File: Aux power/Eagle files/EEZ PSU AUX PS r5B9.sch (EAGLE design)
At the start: 78 parts, among them IC16 LM25575, IC17 MC7812, IC18 TPD4E002DRLR, IC19 TPD2E001DZDR, IC20 ADUM3160BRWZ, Q20 BTA26-600, Q21 BTA26-600, Q22 IRLL014N, X10 826629-5, X11 2411-01, X4 282836-5, X5 09185067324, X6 22-23-2031, X7 LMJ2138812S0LOT6C, X8 826629-8, X9 826629-5

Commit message: AUX PS r5B9
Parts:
- removed B1: DF01S, rectifier:DF01S
- removed C104: 100n, rcl:C-EUC0603
- removed C84: 6n8 (X1), rcl:C-EU102-064X133
- removed FB7: 60R@100MHz, MyLib6:FERRITE_BEAD0603
- removed IC20: ADUM3160BRWZ, MyLib6:ADUM3160BRWZWIDE
- removed R102: 15R/7W, EEZ_Lib1:R_EU7W
- removed R103, R106: 330R/2W, rcl:R-EU_R2512
- removed R104: 270R, rcl:R-EU_R0805
- removed R105: 150R/2W, rcl:R-EU_R2512
- added FB4: 60R@100MHz, MyLib6:FERRITE_BEAD0603
- added R122: 2K2, rcl:R-EU_R0805
- added R123: 16K, rcl:R-EU_R0805
- added R124, R125, R131: 10K, rcl:R-EU_R0805
- added R126: 1K8, rcl:R-EU_R0805
- added R127: 100R, rcl:R-EU_R0805
- added R128: 47K, rcl:R-EU_R0805
- added R129: 1K, rcl:R-EU_R0805
- added R130: 5K6, rcl:R-EU_R0805
- added R132, R133: 22R, rcl:R-EU_R0805
- C85: value 47n/400V -> 6n8 (X1); device rcl:C-EU075-052X106 -> rcl:C-EU102-064X133
- C86: value 22n -> 47n/400V; device rcl:C-EUC0805 -> rcl:C-EU075-052X106
- C87: value 4u7 -> 22n; device rcl:C-EUC1210 -> rcl:C-EUC0805
- C88: value 1mF/25V -> 4u7; device EEZ_Lib1:ECAP5G_10.5MM -> rcl:C-EUC1210
- C91: device rcl:C-EUC0805 -> rcl:C-EUC0603
- C97: value 10u -> 100u; device MyLib6:ECAPPANASONIC_C -> EEZ_Lib1:ECAPPANASONIC_H
- C98: value 100u -> 47n; device EEZ_Lib1:ECAPPANASONIC_H -> rcl:C-EUC0805
- C99: value 47n -> 100n; device rcl:C-EUC0805 -> rcl:C-EUC0603
- IC16: value LM25575 -> LM25575MH/NOPB
- IC17: value MC7812 -> TPD4E002DRLR; device EEZ_Lib1:MC78XX -> EEZ_Lib1:TPD4E002DRLR
- IC18: value TPD4E002DRLR -> TPD2E001DZDR; device EEZ_Lib1:TPD4E002DRLR -> EEZ_Lib1:TPD2E001DZDR
- IC19: value TPD2E001DZDR -> ADUM3160BRWZ; device EEZ_Lib1:TPD2E001DZDR -> MyLib6:ADUM3160BRWZWIDE
- L9: value 100uH (MSS1260-104K) -> 100uH
- R107: value 270R -> 15R/7W; device rcl:R-EU_R0805 -> EEZ_Lib1:R_EU7W
- R108: value 15K -> 330R/2W; device rcl:R-EU_R0805 -> rcl:R-EU_R2512
- R109: value 2K2 -> 330R/2W; device rcl:R-EU_R0805 -> rcl:R-EU_R2512
- R110: value 10R -> 2K2; device rcl:R-EU_R1206 -> rcl:R-EU_R0805
- R111: value 5K6 1% -> 2K2
- R112: value 18K -> 330R/2W; device rcl:R-EU_R0805 -> rcl:R-EU_R2512
- R113: value 20K -> 49R9
- R114: value 1K8 1% -> 220R
- R115: value 100R -> 330R/2W; device rcl:R-EU_R0805 -> rcl:R-EU_R2512
- R116: value 47K -> 49R9
- R117: value 1K -> 220R
- R118: value 5K6 -> 16K
- R119: value 10K -> 2K2
- R120: value 22R -> 10R; device rcl:R-EU_R0805 -> rcl:R-EU_R1206
- R121: value 22R -> 5K6
- TR2: value TEZ6/D230/15V -> VTX-214-005-112 (or MYRRA 47154); device EEZ_Lib1:PCB_TRAFO6VA_TEZ+VPP+MYRRA -> EEZ_Lib1:AC_DC_ADAPTER_5W
- X4: value 282836-5 -> 39303055; device EEZ_Lib1:TBLOCK5.0_5A -> EEZ_Lib1:MINIFIT_6659-5
- X7: value LMJ2138812S0LOT6C -> LMJ2138814S0L1T1C; device EEZ_Lib1:RJ45-VERT -> EEZ_Lib1:RJ45-VERTLMJ2138814S0L1T1C
- renumbered U$13 to FM3, U$14 to FM4
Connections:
- removed net 12VDC: C97.+, C98.+, D20.C, IC17.VO, X6-1.S
- removed net N$78: B1.AC1, TR2.S1
- removed net N$80: B1.AC2, TR2.S2
- removed net N$82: Q21.A2, R102.2, R103.2, R105.1, X4-3.1
- new net N$152: Q20.A1, R107.2, R110.1
- new net N$169: R122.1, R123.2
- new net N$171: R124.2, R125.1
- new net N$174: OK2.C, R116.1
- new net N$175: OK1.C, R113.1
- net +5V: now also C99.1, IC19.VBUS2, R121.1, R130.1; no longer C100.1, IC20.VBUS2, R111.1, R118.1
- net AC_EARTH: now also FB6.1; no longer FB7.1
- net AC_IN1_MAIN: now also C85.1, R107.1, R111.2, TR2.IN2; no longer C84.1, Q20.A1, TR2.P2
- net AC_IN2_MAIN: now also C85.2, C86.1, TR2.IN1; no longer C84.2, C85.1, TR2.P1
- net AUX_+3V3: now also FB4.2; no longer FB5.2
- net AUX_ETH_IN+: now also IC17.IO3; no longer IC18.IO4
- net AUX_ETH_IN-: now also IC17.IO4; no longer IC18.IO3
- net AUX_ETH_OUT+: now also IC17.IO1; no longer IC18.IO2
- net AUX_ETH_OUT-: now also IC17.IO2; no longer IC18.IO1
- net AUX_FAN_CTRL: now also R127.2; no longer R115.2
- net AUX_FAN_SENSE: now also R130.2, R131.1; no longer R118.2, R119.1
- net AUX_PWR_DIRECT: now also R114.2; no longer R104.2
- net AUX_PWR_SSTART: now also R117.2; no longer R107.2
- net D+: now also IC18.IO1, R133.1; no longer IC19.IO1, R121.1
- net D-: now also IC18.IO2, R132.1; no longer IC19.IO2, R120.1
- net DC_PREG2: now also C88.1, R118.2; no longer C87.1, R108.2
- net FAN_OUT: now also C98.2; no longer C99.2
- net GND: now also C102.2, C88.2, C99.2, IC19.GND2, IC19.GND2_2, R119.1, R122.2, R126.2, R128.1, R129.1, R131.2, TR2.-; no longer B1.-, C100.2, C103.2, C87.2, C88.-, C97.-, IC18.GND, IC20.GND2, IC20.GND2_2, R109.1, R112.2, R114.2, R116.1, R117.1, R119.2
- net IS1: now also R120.1; no longer R110.1
- net MCU_D+: now also IC19.DD+; no longer IC20.DD+
- net MCU_D-: now also IC19.DD-; no longer IC20.DD-
- net N$125: now also FB4.1; no longer FB5.1
- net N$52: now also R125.2; no longer R113.2
- net N$57: now also R121.2, R126.1; no longer R111.2, R114.1
- net N$58: now also C87.2; no longer C86.2
- net N$59: now also R124.1; no longer R113.1
- net N$60: now also R123.1; no longer R112.1
- net N$69: now also R118.1, R119.2; no longer R108.1, R109.2
- net N$70: now also R120.2; no longer R110.2
- net N$71: now also R111.1
- net N$72: now also R110.2
- net N$73: now also R115.1; no longer R106.1
- net N$74: now also R113.2, R114.1; no longer OK1.C, R104.1
- net N$75: now also R116.2, R117.1; no longer OK2.C, R107.1
- net N$76: now also R112.1; no longer R103.1
- net N$81: now also Q21.A2, R108.1, R109.1, R112.2, R115.2, X4-3.1; no longer R102.1, R106.2
- net N$83: now also C86.2, R108.2, R109.2; no longer C85.2, R105.2
- net N$84: now also C98.1, R129.2; no longer C99.1, R117.2
- net N$85: now also R127.1, R128.2; no longer R115.1, R116.2
- net N$86: now also C97.-; no longer C98.-
- net N$87: now also C103.1, IC19.PDEN, IC19.SPU, IC19.VDD1; no longer C104.1, IC20.PDEN, IC20.SPU, IC20.VDD1
- net N$88: now also IC19.UD-, R132.2; no longer IC20.UD-, R120.2
- net N$89: now also IC19.UD+, R133.2; no longer IC20.UD+, R121.2
- net N$90: now also C100.1, FB5.2, IC19.VBUS1; no longer C101.1, FB6.2, IC20.VBUS1
- net N$91: now also C102.1, IC19.PIN, IC19.SPD, IC19.VDD2; no longer C103.1, IC20.PIN, IC20.SPD, IC20.VDD2
- net SW2: now also C87.1; no longer C86.1
- net VIN: now also C97.+, D20.C, TR2.+, X6-1.S; no longer B1.+, C88.+, IC17.VI
- net XUSB_GND: now also C100.2, C101.1, C103.2, FB6.2, IC18.GND, IC19.GND1, IC19.GND1_2; no longer C101.2, C102.1, C104.2, FB7.2, IC19.GND, IC20.GND1, IC20.GND1_2
- net XUSB_VBUS: now also C101.2, FB5.1, IC18.VCC; no longer C102.2, FB6.1, IC19.VCC
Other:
- note added: "SRU1038-101Y or DE1207-100"
- note removed: "or DE1207-100"
- moved on the sheet: C100, C101, C102, C103, C85, C86, C87, C90, C91, C92, C93, C94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

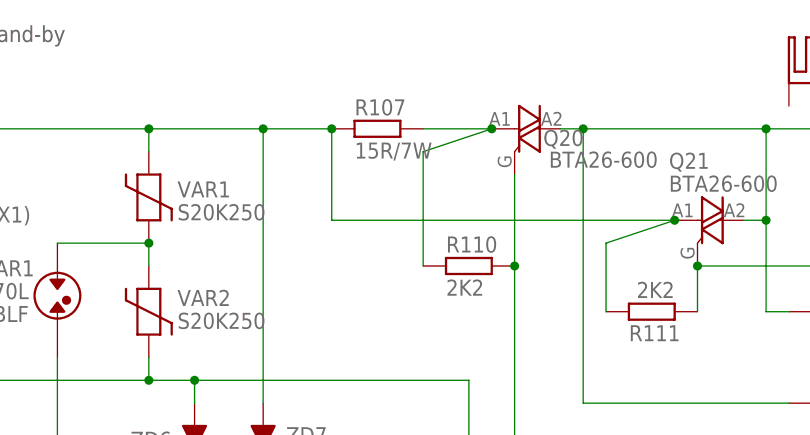
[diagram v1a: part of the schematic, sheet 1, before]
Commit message: AUX PS: R107 value changed
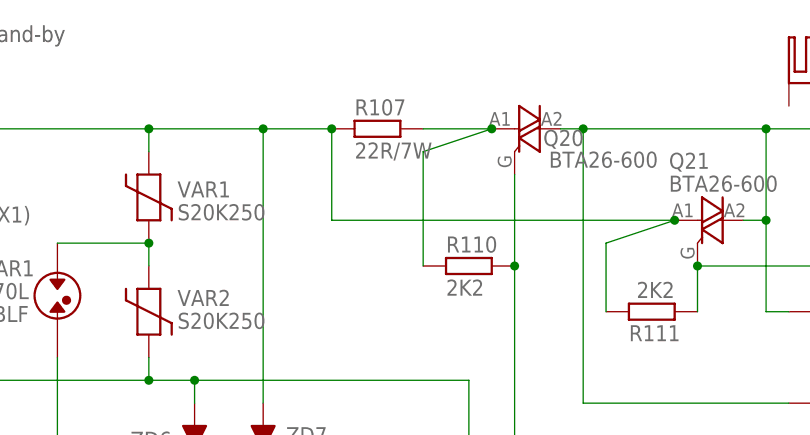
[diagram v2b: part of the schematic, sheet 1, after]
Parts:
- R107: value 15R/7W -> 22R/7W
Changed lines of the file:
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@@
 <part name="R108" library="rcl" deviceset="R-EU_" device="R2512" value="330R/2W"/>
 <part name="C86" library="rcl" deviceset="C-EU" device="075-052X106" value="47n/400V"/>
-<part name="R107" library="EEZ_Lib1" deviceset="R_EU" device="7W" value="15R/7W"/>
+<part name="R107" library="EEZ_Lib1" deviceset="R_EU" device="7W" value="22R/7W"/>
 <part name="KK1" library="EEZ_Lib1" deviceset="SK145" device="" value="SK 145/37,5"/>
 <part name="OK1" library="EEZ_Lib1" deviceset="MOC305X" device="" value="MOC3052"/>
